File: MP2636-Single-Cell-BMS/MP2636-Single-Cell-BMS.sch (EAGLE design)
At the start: 0 parts

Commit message: MP2636 added
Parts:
- added U1: MP2636GR-P, MP2636GR-P:MP2636GR-P
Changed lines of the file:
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@@
 <parts>
 <part name="FRAME1" library="frames" deviceset="A4L-LOC" device=""/>
+<part name="U1" library="MP2636GR-P" deviceset="MP2636GR-P" device=""/>
 </parts>
 <sheets>
@@
 <attribute name="SHEET" x="230.505" y="5.08" size="2.54" layer="94"/>
 </instance>
+<instance part="U1" gate="G$1" x="106.68" y="71.12" smashed="yes">
+<attribute name="NAME" x="101.6" y="122.428" size="1.778" layer="95"/>
+<attribute name="VALUE" x="101.6" y="68.58" size="1.778" layer="96"/>
+</instance>
 </instances>

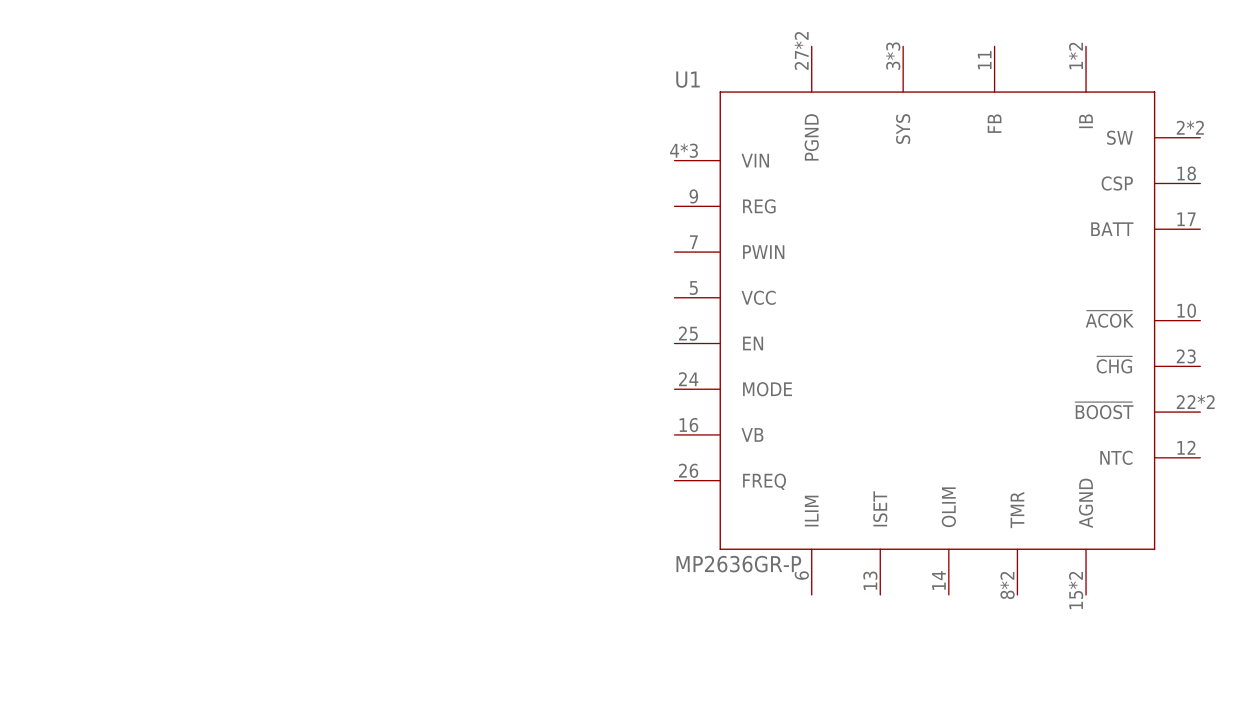
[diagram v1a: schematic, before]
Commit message: Operation mode is added
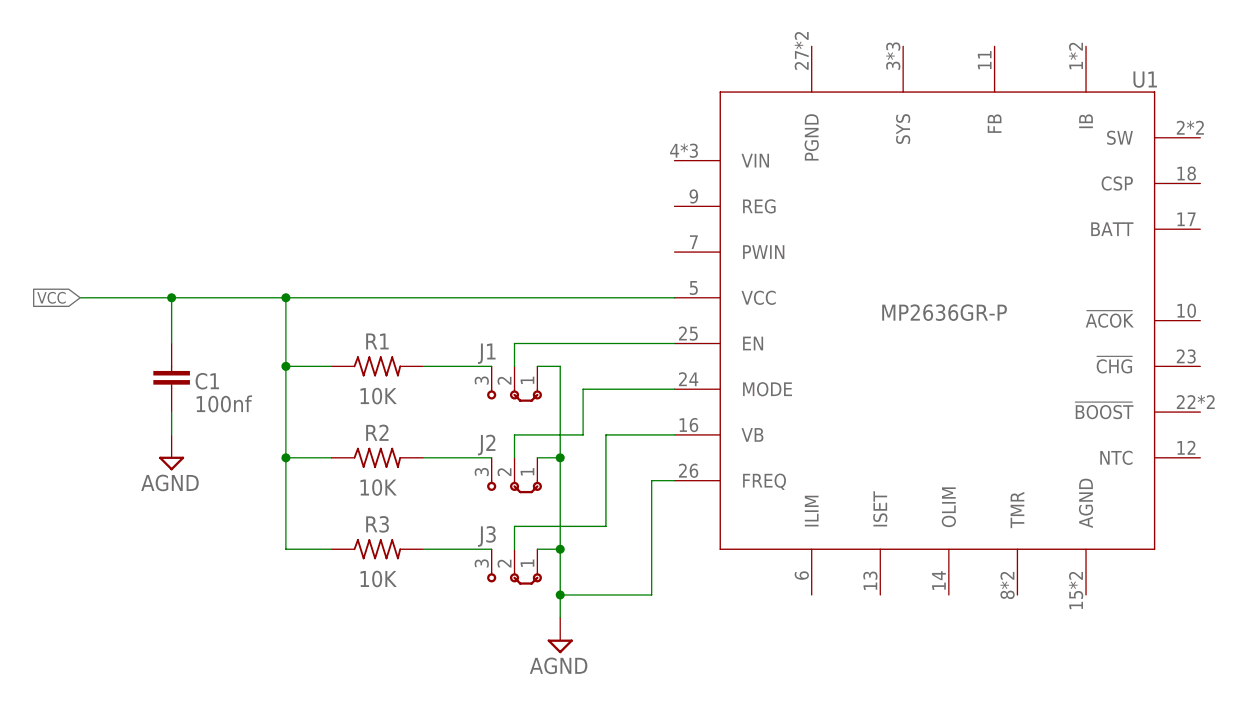
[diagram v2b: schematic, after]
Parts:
- added C1: 100nf, Capacitor:C_CHIP-0805(2012-METRIC)
- added J1, J2, J3: (no value), jumper:J2X2MM
- added R1, R2, R3: 10K, Resistor:R-US_CHIP-0805(2012-METRIC)
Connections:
- new net DGND: C1.2, J1.1, J2.1, J3.1, U1.FREQ
- new net N$2: J1.3, R1.2
- new net N$3: J1.2, U1.EN
- new net N$4: J2.2, U1.MODE
- new net N$5: J3.2, U1.VB
- new net N$6: J2.3, R2.2
- new net N$7: J3.3, R3.2
- new net VCC: C1.1, R1.1, R2.1, R3.1, U1.VCC
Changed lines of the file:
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@@
 <layer number="97" name="Info" color="7" fill="1" visible="yes" active="yes"/>
 <layer number="98" name="Guide" color="6" fill="1" visible="yes" active="yes"/>
+<layer number="99" name="SpiceOrder" color="7" fill="1" visible="yes" active="yes"/>
 </layers>
 <schematic xreflabel="%F%N/%S.%C%R" xrefpart="/%S.%C%R">
@@
 <part name="FRAME1" library="frames" deviceset="A4L-LOC" device=""/>
 <part name="U1" library="MP2636GR-P" deviceset="MP2636GR-P" device=""/>
+<part name="C1" library="Capacitor" deviceset="C" device="CHIP-0805(2012-METRIC)" package3d_urn="urn:adsk.eagle:package:16290897/2" technology="_" value="100nf"/>
+<part name="SUPPLY1" library="Power_Symbols" deviceset="AGND" device="" value="AGND"/>
+<part name="R1" library="Resistor" deviceset="R-US" device="CHIP-0805(2012-METRIC)" package3d_urn="urn:adsk.eagle:package:16378559/2" technology="_" value="10K"/>
+<part name="R2" library="Resistor" deviceset="R-US" device="CHIP-0805(2012-METRIC)" package3d_urn="urn:adsk.eagle:package:16378559/2" technology="_" value="10K"/>
+<part name="R3" library="Resistor" deviceset="R-US" device="CHIP-0805(2012-METRIC)" package3d_urn="urn:adsk.eagle:package:16378559/2" technology="_" value="10K"/>
+<part name="J1" library="jumper" deviceset="J2" device="X2MM" package3d_urn="urn:adsk.eagle:package:15506/1"/>
+<part name="J2" library="jumper" deviceset="J2" device="X2MM" package3d_urn="urn:adsk.eagle:package:15506/1"/>
+<part name="J3" library="jumper" deviceset="J2" device="X2MM" package3d_urn="urn:adsk.eagle:package:15506/1"/>
+<part name="SUPPLY2" library="Power_Symbols" deviceset="AGND" device="" value="AGND"/>
 </parts>
 <sheets>
@@
 </instance>
 <instance part="U1" gate="G$1" x="106.68" y="71.12" smashed="yes">
-<attribute name="NAME" x="101.6" y="122.428" size="1.778" layer="95"/>
-<attribute name="VALUE" x="101.6" y="68.58" size="1.778" layer="96"/>
+<attribute name="NAME" x="152.4" y="122.428" size="1.778" layer="95"/>
+<attribute name="VALUE" x="124.46" y="96.52" size="1.778" layer="96"/>
+</instance>
+<instance part="C1" gate="G$1" x="45.72" y="91.44" smashed="yes">
+<attribute name="NAME" x="48.26" y="88.9" size="1.778" layer="95"/>
+<attribute name="VALUE" x="48.26" y="86.36" size="1.778" layer="96"/>
+</instance>
+<instance part="SUPPLY1" gate="G$1" x="45.72" y="81.28" smashed="yes">
+<attribute name="VALUE" x="45.593" y="77.597" size="1.778" layer="96" align="bottom-center"/>
+</instance>
+<instance part="R1" gate="G$1" x="68.58" y="91.44" smashed="yes">
+<attribute name="NAME" x="68.58" y="94.2086" size="1.778" layer="95" align="center"/>
+<attribute name="VALUE" x="68.58" y="88.138" size="1.778" layer="96" align="center"/>
+</instance>
+<instance part="R2" gate="G$1" x="68.58" y="81.28" smashed="yes">
+<attribute name="NAME" x="68.58" y="84.0486" size="1.778" layer="95" align="center"/>
+<attribute name="VALUE" x="68.58" y="77.978" size="1.778" layer="96" align="center"/>
+</instance>
+<instance part="R3" gate="G$1" x="68.58" y="71.12" smashed="yes">
+<attribute name="NAME" x="68.58" y="73.8886" size="1.778" layer="95" align="center"/>
+<attribute name="VALUE" x="68.58" y="67.818" size="1.778" layer="96" align="center"/>
+</instance>
+<instance part="J1" gate="G$1" x="83.82" y="88.9" smashed="yes" rot="R270">
+<attribute name="NAME" x="81.915" y="93.98" size="1.778" layer="95" rot="R180"/>
+<attribute name="VALUE" x="81.28" y="86.995" size="1.778" layer="96" rot="R270"/>
+</instance>
+<instance part="J2" gate="G$1" x="83.82" y="78.74" smashed="yes" rot="R270">
+<attribute name="NAME" x="81.915" y="83.82" size="1.778" layer="95" rot="R180"/>
+<attribute name="VALUE" x="81.28" y="76.835" size="1.778" layer="96" rot="R270"/>
+</instance>
+<instance part="J3" gate="G$1" x="83.82" y="68.58" smashed="yes" rot="R270">
+<attribute name="NAME" x="81.915" y="73.66" size="1.778" layer="95" rot="R180"/>
+<attribute name="VALUE" x="81.28" y="66.675" size="1.778" layer="96" rot="R270"/>
+</instance>
+<instance part="SUPPLY2" gate="G$1" x="88.9" y="60.96" smashed="yes">
+<attribute name="VALUE" x="88.773" y="57.277" size="1.778" layer="96" align="bottom-center"/>
 </instance>
 </instances>
@@
 </busses>
 <nets>
+<net name="VCC" class="0">
+<segment>
+<pinref part="U1" gate="G$1" pin="VCC"/>
+<wire x1="101.6" y1="99.06" x2="58.42" y2="99.06" width="0.1524" layer="91"/>
+<pinref part="C1" gate="G$1" pin="1"/>
+<wire x1="58.42" y1="99.06" x2="45.72" y2="99.06" width="0.1524" layer="91"/>
+<wire x1="45.72" y1="93.98" x2="45.72" y2="99.06" width="0.1524" layer="91"/>
+<junction x="45.72" y="99.06"/>
+<pinref part="R1" gate="G$1" pin="1"/>
+<wire x1="63.5" y1="91.44" x2="58.42" y2="91.44" width="0.1524" layer="91"/>
+<wire x1="58.42" y1="91.44" x2="58.42" y2="99.06" width="0.1524" layer="91"/>
+<junction x="58.42" y="99.06"/>
+<wire x1="58.42" y1="91.44" x2="58.42" y2="81.28" width="0.1524" layer="91"/>
+<junction x="58.42" y="91.44"/>
+<pinref part="R2" gate="G$1" pin="1"/>
+<wire x1="58.42" y1="81.28" x2="63.5" y2="81.28" width="0.1524" layer="91"/>
+<wire x1="58.42" y1="81.28" x2="58.42" y2="71.12" width="0.1524" layer="91"/>
+<junction x="58.42" y="81.28"/>
+<pinref part="R3" gate="G$1" pin="1"/>
+<wire x1="58.42" y1="71.12" x2="63.5" y2="71.12" width="0.1524" layer="91"/>
+<wire x1="35.56" y1="99.06" x2="45.72" y2="99.06" width="0.1524" layer="91"/>
+<label x="35.56" y="99.06" size="1.27" layer="95" rot="R180" xref="yes"/>
+</segment>
+</net>
+<net name="DGND" class="0">
+<segment>
+<pinref part="C1" gate="G$1" pin="2"/>
+<wire x1="45.72" y1="86.36" x2="45.72" y2="83.82" width="0.1524" layer="91"/>
+<pinref part="SUPPLY1" gate="G$1" pin="AGND"/>
+</segment>
+<segment>
+<pinref part="J1" gate="G$1" pin="1"/>
+<wire x1="86.36" y1="91.44" x2="88.9" y2="91.44" width="0.1524" layer="91"/>
+<wire x1="88.9" y1="91.44" x2="88.9" y2="81.28" width="0.1524" layer="91"/>
+<pinref part="J2" gate="G$1" pin="1"/>
+<wire x1="88.9" y1="81.28" x2="86.36" y2="81.28" width="0.1524" layer="91"/>
+<wire x1="88.9" y1="81.28" x2="88.9" y2="71.12" width="0.1524" layer="91"/>
+<junction x="88.9" y="81.28"/>
+<pinref part="J3" gate="G$1" pin="1"/>
+<wire x1="88.9" y1="71.12" x2="86.36" y2="71.12" width="0.1524" layer="91"/>
+<wire x1="88.9" y1="71.12" x2="88.9" y2="66.04" width="0.1524" layer="91"/>
+<junction x="88.9" y="71.12"/>
+<pinref part="U1" gate="G$1" pin="FREQ"/>
+<wire x1="88.9" y1="66.04" x2="88.9" y2="63.5" width="0.1524" layer="91"/>
+<wire x1="101.6" y1="78.74" x2="99.06" y2="78.74" width="0.1524" layer="91"/>
+<wire x1="99.06" y1="78.74" x2="99.06" y2="66.04" width="0.1524" layer="91"/>
+<wire x1="99.06" y1="66.04" x2="88.9" y2="66.04" width="0.1524" layer="91"/>
+<junction x="88.9" y="66.04"/>
+<pinref part="SUPPLY2" gate="G$1" pin="AGND"/>
+</segment>
+</net>
+<net name="N$2" class="0">
+<segment>
+<pinref part="R1" gate="G$1" pin="2"/>
+<pinref part="J1" gate="G$1" pin="3"/>
+<wire x1="73.66" y1="91.44" x2="81.28" y2="91.44" width="0.1524" layer="91"/>
+</segment>
+</net>
+<net name="N$3" class="0">
+<segment>
+<pinref part="J1" gate="G$1" pin="2"/>
+<wire x1="83.82" y1="91.44" x2="83.82" y2="93.98" width="0.1524" layer="91"/>
+<pinref part="U1" gate="G$1" pin="EN"/>
+<wire x1="83.82" y1="93.98" x2="101.6" y2="93.98" width="0.1524" layer="91"/>
+</segment>
+</net>
+<net name="N$4" class="0">
+<segment>
+<pinref part="J2" gate="G$1" pin="2"/>
+<wire x1="83.82" y1="81.28" x2="83.82" y2="83.82" width="0.1524" layer="91"/>
+<wire x1="83.82" y1="83.82" x2="91.44" y2="83.82" width="0.1524" layer="91"/>
+<wire x1="91.44" y1="83.82" x2="91.44" y2="88.9" width="0.1524" layer="91"/>
+<pinref part="U1" gate="G$1" pin="MODE"/>
+<wire x1="91.44" y1="88.9" x2="101.6" y2="88.9" width="0.1524" layer="91"/>
+</segment>
+</net>
+<net name="N$5" class="0">
+<segment>
+<pinref part="J3" gate="G$1" pin="2"/>
+<wire x1="83.82" y1="71.12" x2="83.82" y2="73.66" width="0.1524" layer="91"/>
+<wire x1="83.82" y1="73.66" x2="93.98" y2="73.66" width="0.1524" layer="91"/>
+<wire x1="93.98" y1="73.66" x2="93.98" y2="83.82" width="0.1524" layer="91"/>
+<pinref part="U1" gate="G$1" pin="VB"/>
+<wire x1="93.98" y1="83.82" x2="101.6" y2="83.82" width="0.1524" layer="91"/>
+</segment>
+</net>
+<net name="N$6" class="0">
+<segment>
+<pinref part="R2" gate="G$1" pin="2"/>
+<pinref part="J2" gate="G$1" pin="3"/>
+<wire x1="73.66" y1="81.28" x2="81.28" y2="81.28" width="0.1524" layer="91"/>
+</segment>
+</net>
+<net name="N$7" class="0">
+<segment>
+<pinref part="R3" gate="G$1" pin="2"/>
+<pinref part="J3" gate="G$1" pin="3"/>
+<wire x1="73.66" y1="71.12" x2="81.28" y2="71.12" width="0.1524" layer="91"/>
+</segment>
+</net>
 </nets>
 </sheet>
@@
 will not be understood (or retained) with this version.
 </note>
+<note version="8.3" severity="warning">
+Since Version 8.3, EAGLE supports the association of 3D packages
+with devices in libraries, schematics, and board files. Those 3D
+packages will not be understood (or retained) with this version.
+</note>
+<note version="8.4" severity="warning">
+Since Version 8.4, EAGLE supports properties for SPICE simulation.
+Probes in schematics and SPICE mapping objects found in parts and library devices
+will not be understood with this version. Update EAGLE to the latest version
+for full support of SPICE simulation.
+</note>
 </compatibility>

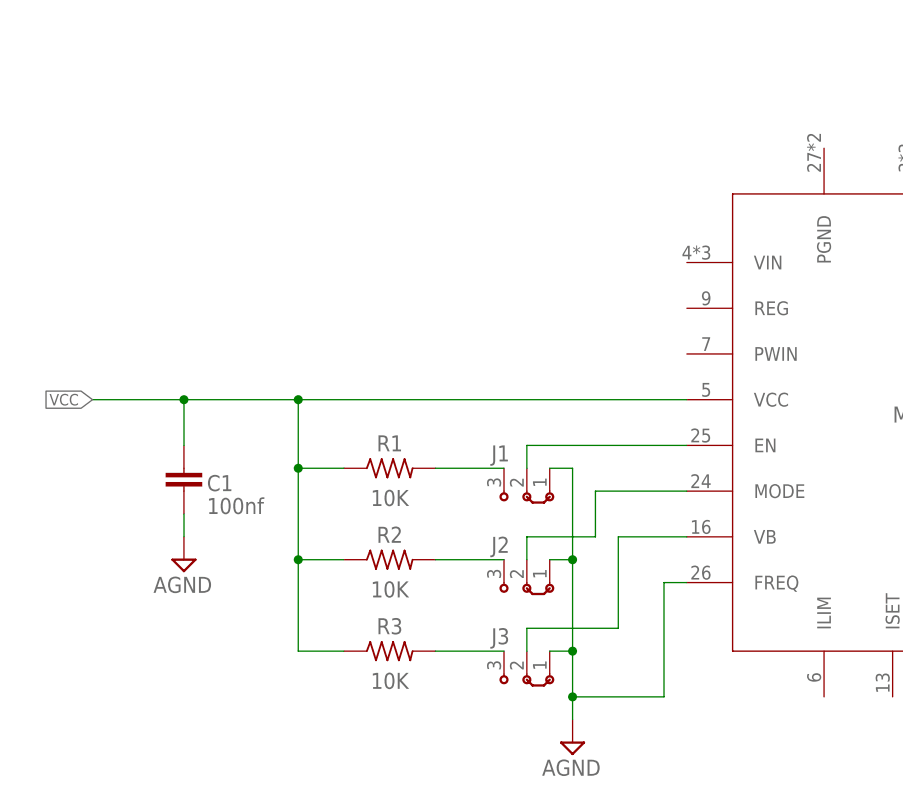
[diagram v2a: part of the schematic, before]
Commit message: Input circuit is added
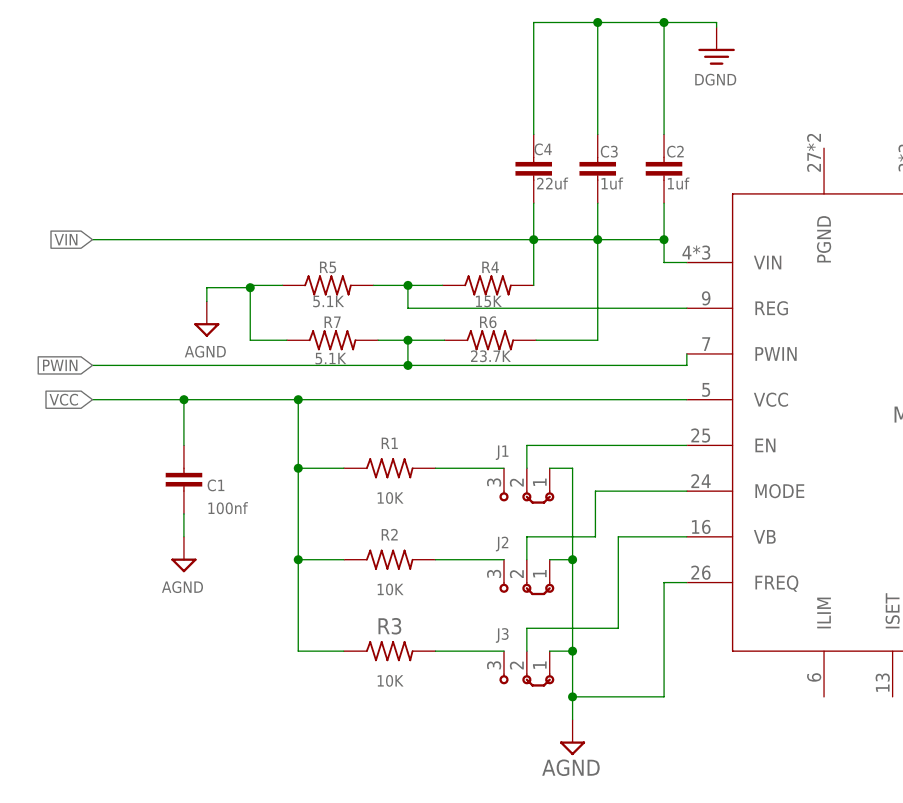
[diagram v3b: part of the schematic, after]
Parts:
- added C2, C3: 1uf, Capacitor:C_CHIP-0805(2012-METRIC)
- added C4: 22uf, Capacitor:C_CHIP-0805(2012-METRIC)
- added R4: 15K, Resistor:R-US_CHIP-0805(2012-METRIC)
- added R5, R7: 5.1K, Resistor:R-US_CHIP-0805(2012-METRIC)
- added R6: 23.7K, Resistor:R-US_CHIP-0805(2012-METRIC)
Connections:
- new net AGND: R5.1, R7.1
- new net N$8: R4.1, R5.2, U1.REG
- new net PWIN: R6.1, R7.2, U1.PWIN
- new net VIN: C2.2, C3.2, C4.2, R4.2, R6.2, U1.VIN
- net DGND: now also C2.1, C3.1, C4.1
